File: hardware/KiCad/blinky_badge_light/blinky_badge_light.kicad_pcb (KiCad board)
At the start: 4 copper layers, 108.6 x 87.8 mm, 108 parts, among them Q2 Q_PMOS_GSD, SW1 TS-1187A-B-A-B, U1 ESP32-S3-WROOM-1, U2 TP4056, U3 AP2112K-3.3, U4 MT3608, U5 CP2102N-Axx-xQFN24, U6 SN74LVC1T45DBV

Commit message: adding plus and minus to inside battery holder so it's easier to see which direction to use
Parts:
- added G***: LOGO, labels:minus, B.Cu at (119.3, 82.1)
- added G***: LOGO, labels:plus, B.Cu at (180.2, 82.1)
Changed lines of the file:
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@@
+		(embedded_fonts no)
+	)
+	(footprint "labels:minus"
+		(layer "B.Cu")
+		(at 119.251036 82.058777)
+		(property "Reference" "G***"
+			(at 0 0 180)
+			(layer "F.SilkS")
+			(hide yes)
+			(effects
+				(font
+					(size 1.5 1.5)
+					(thickness 0.3)
+				)
+			)
+		)
+		(property "Value" "LOGO"
+			(at 0.75 0 180)
+			(layer "F.SilkS")
+			(hide yes)
+			(effects
+				(font
+					(size 1.5 1.5)
+					(thickness 0.3)
+				)
+			)
+		)
+		(property "Datasheet" ""
+			(at 0 0 180)
+			(layer "B.Fab")
+			(hide yes)
+			(effects
+				(font
+					(size 1.27 1.27)
+					(thickness 0.15)
+				)
+				(justify mirror)
+			)
+		)
+		(property "Description" ""
+			(at 0 0 180)
+			(layer "B.Fab")
+			(hide yes)
+			(effects
+				(font
+					(size 1.27 1.27)
+					(thickness 0.15)
+				)
+				(justify mirror)
+			)
+		)
+		(attr board_only exclude_from_pos_files exclude_from_bom)
+		(fp_poly
+			(pts
+				(xy -0.286687 -0.690521) (xy 0.090711 -0.696229) (xy 1.390739 -0.719666) (xy 1.515832 -0.942743)
+				(xy 1.593212 -1.119444) (xy 1.569107 -1.263259) (xy 1.495844 -1.387243) (xy 1.350762 -1.608666)
+				(xy 0.053503 -1.608666) (xy -0.449903 -1.606654) (xy -0.811495 -1.598645) (xy -1.058768 -1.581677)
+				(xy -1.219213 -1.552788) (xy -1.320324 -1.509018) (xy -1.383879 -1.453832) (xy -1.510433 -1.211294)
+				(xy -1.479872 -0.965652) (xy -1.366659 -0.815185) (xy -1.284805 -0.760109) (xy -1.163403 -0.722351)
+				(xy -0.97493 -0.699665) (xy -0.691865 -0.689803)
+			)
+			(stroke
+				(width 0)
+				(type solid)
+			)
+			(fill yes)
+			(layer "B.SilkS")
+		)
 		(embedded_fonts no)
 	)
@@
 		)
 	)
+	(footprint "labels:plus"
+		(layer "B.Cu")
+		(at 180.21152 82.063129)
+		(property "Reference" "G***"
+			(at 0 0 180)
+			(layer "F.SilkS")
+			(hide yes)
+			(effects
+				(font
+					(size 1.5 1.5)
+					(thickness 0.3)
+				)
+			)
+		)
+		(property "Value" "LOGO"
+			(at 0.75 0 180)
+			(layer "F.SilkS")
+			(hide yes)
+			(effects
+				(font
+					(size 1.5 1.5)
+					(thickness 0.3)
+				)
+			)
+		)
+		(property "Datasheet" ""
+			(at 0 0 180)
+			(layer "B.Fab")
+			(hide yes)
+			(effects
+				(font
+					(size 1.27 1.27)
+					(thickness 0.15)
+				)
+				(justify mirror)
+			)
+		)
+		(property "Description" ""
+			(at 0 0 180)
+			(layer "B.Fab")
+			(hide yes)
+			(effects
+				(font
+					(size 1.27 1.27)
+					(thickness 0.15)
+				)
+				(justify mirror)
+			)
+		)
+		(attr board_only exclude_from_pos_files exclude_from_bom)
+		(fp_poly
+			(pts
+				(xy 0.322711 1.607171) (xy 0.466663 1.523091) (xy 0.562701 1.353457) (xy 0.621675 1.074135) (xy 0.654437 0.660986)
+				(xy 0.663657 0.420523) (xy 0.692314 -0.507999) (xy 1.560701 -0.507999) (xy 1.968384 -0.51241) (xy 2.241811 -0.529217)
+				(xy 2.415912 -0.563784) (xy 2.525616 -0.621474) (xy 2.56921 -0.662833) (xy 2.695614 -0.904885) (xy 2.666152 -1.149983)
+				(xy 2.554499 -1.29921) (xy 2.443165 -1.366708) (xy 2.266689 -1.409464) (xy 1.991479 -1.432114) (xy 1.583946 -1.439288)
+				(xy 1.538499 -1.439333) (xy 0.677333 -1.439333) (xy 0.676084 -2.264833) (xy 0.663726 -2.695063)
+				(xy 0.630758 -3.043722) (xy 0.581262 -3.271525) (xy 0.56832 -3.301999) (xy 0.395917 -3.480139) (xy 0.155788 -3.546055)
+				(xy -0.085557 -3.490747) (xy -0.194827 -3.405274) (xy -0.261988 -3.298771) (xy -0.305231 -3.135068)
+				(xy -0.329105 -2.880577) (xy -0.338158 -2.501709) (xy -0.338667 -2.342832) (xy -0.338667 -1.439333)
+				(xy -1.259634 -1.439333) (xy -1.720069 -1.432163) (xy -2.037288 -1.403587) (xy -2.237063 -1.343005)
+				(xy -2.345167 -1.239817) (xy -2.387371 -1.083422) (xy -2.391834 -0.973666) (xy -2.374402 -0.784292)
+				(xy -2.304924 -0.653822) (xy -2.157627 -0.571656) (xy -1.90674 -0.527193) (xy -1.526491 -0.509835)
+				(xy -1.259634 -0.507999) (xy -0.338667 -0.507999) (xy -0.338667 0.407152) (xy -0.329193 0.894518)
+				(xy -0.294911 1.23673) (xy -0.227037 1.457207) (xy -0.116785 1.57937) (xy 0.044629 1.626638) (xy 0.119995 1.629834)
+			)
+			(stroke
+				(width 0)
+				(type solid)
+			)
+			(fill yes)
+			(layer "B.SilkS")
+		)
+		(embedded_fonts no)
+	)
 	(footprint "Capacitor_SMD:C_0402_1005Metric"

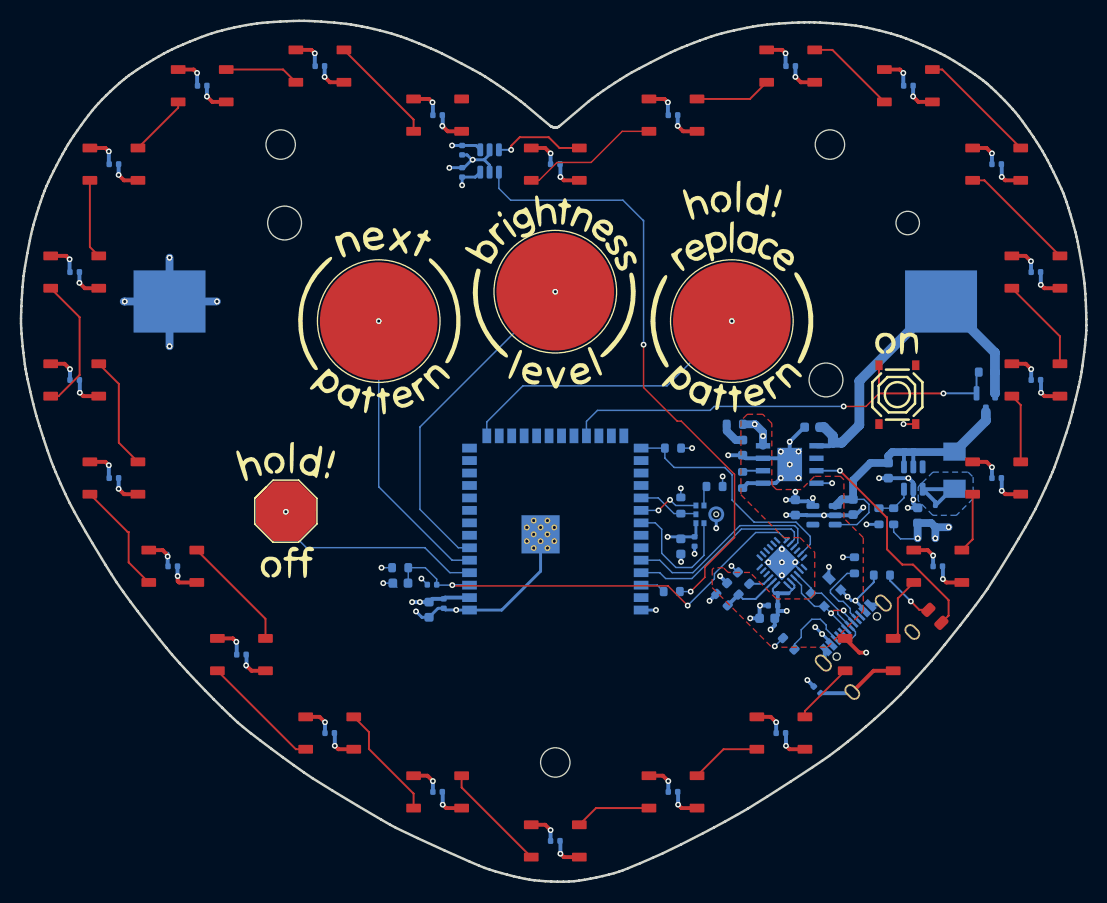
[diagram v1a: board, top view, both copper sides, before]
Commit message: fix symbol used by transistor
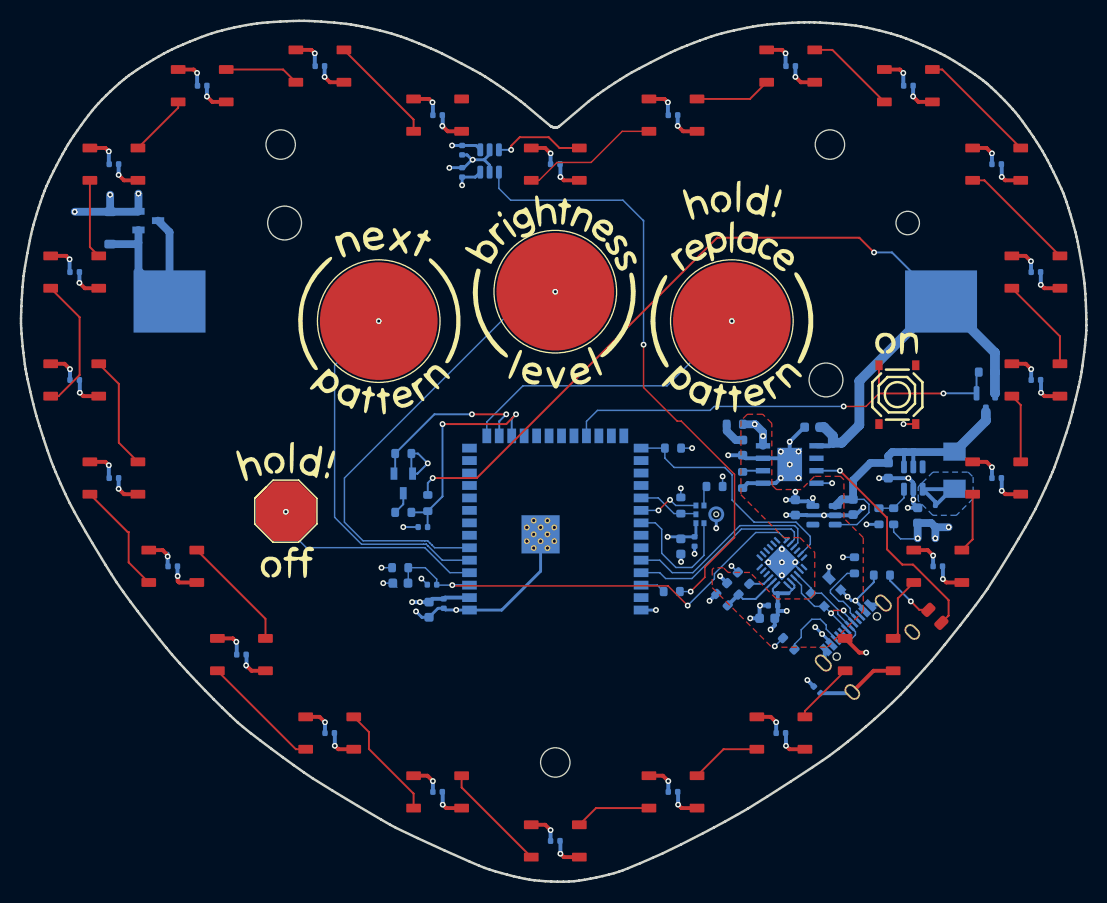
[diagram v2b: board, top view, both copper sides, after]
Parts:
- removed the G*** at (125.0, 98.5)
- added C41: 100nF, Capacitor_SMD:C_0402_1005Metric, B.Cu at (136.5, 104.0)
- added D28: ESD Diode, Diode_SMD:D_SOD-123, B.Cu at (104.6, 73.5)
- added Q1: N-Channel MOSFET, footprints:SOT-23-3_L2.9-W1.3-P1.90-LS2.4-BR, B.Cu at (108.5, 72.8)
- added Q3: N-Channel MOSFET, footprints:SOT-23-3_L2.9-W1.3-P1.90-LS2.4-BR, B.Cu at (134.5, 99.5)
- added R13: 100kΩ, Resistor_SMD:R_0603_1608Metric, B.Cu at (137.0, 101.5)
- added R18: 100kΩ, Resistor_SMD:R_0603_1608Metric, B.Cu at (134.5, 102.5)
- added R19: 100kΩ, Resistor_SMD:R_0603_1608Metric, B.Cu at (134.5, 96.5)
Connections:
- BT1 pad 2: GND -> BAT-
- U1 pad 16: unconnected-(U1-GPIO46-Pad16) -> ESP32 Battery Monitoring Control
- U1 pad 17: unconnected-(U1-GPIO9/TOUCH9/ADC1_CH8/FSPIHD/SUBSPIHD-Pad17) -> ESP32 Battery Monitoring
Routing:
- net BAT+: track 35.3 -> 101.9 mm, vias 0 -> 2
- net ESP32 Battery Monitoring: track 0.00 -> 23.2 mm, vias 0 -> 2
- net BAT-: track 0.00 -> 20.1 mm
- net ESP32 Battery Monitoring Control: track 0.00 -> 17.6 mm, vias 0 -> 2
- net Net-(U1-GPIO6/TOUCH6/ADC1_CH5): track 34.6 -> 47.7 mm
- net Net-(U1-GPIO5/TOUCH5/ADC1_CH4): track 29.2 -> 37.4 mm
- net Net-(Q3-D): track 0.00 -> 2.29 mm
- net GND: track 182.2 -> 181.4 mm, vias 66 -> 67

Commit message: moving some stuff around
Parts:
- added TOUCH_5: TestPoint, TestPoint:TestPoint_Pad_D4.0mm, F.Cu at (114.0, 93.0)
- moved Q3 62.4 mm to (186.5, 65.0)
- moved R19 62.4 mm to (186.5, 62.0)
- moved R18 61.4 mm to (185.0, 67.5), turned to 90 degrees
- moved R13 61.3 mm to (188.0, 67.5)
- moved C41 61.3 mm to (186.5, 68.5), turned to 90 degrees
- moved G*** 6.20 mm to (127.1, 106.3)
- moved TOUCH_4 6.20 mm to (126.5, 106.5)
- moved G*** 1.50 mm to (149.5, 81.5)
- moved TOUCH_2 1.50 mm to (150.0, 81.5)
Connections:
- U1 pad 7: unconnected-(U1-GPIO7/TOUCH7/ADC1_CH6-Pad7) -> Net-(U1-GPIO7/TOUCH7/ADC1_CH6)
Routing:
- net BAT+: track 101.9 -> 52.0 mm, vias 2 -> 0
- net ESP32 Battery Monitoring Control: track 17.6 -> 65.4 mm
- net ESP32 Battery Monitoring: track 23.2 -> 60.0 mm
- net Net-(U1-GPIO7/TOUCH7/ADC1_CH6): track 0.00 -> 32.2 mm, vias 0 -> 3
- net Net-(U1-GPIO6/TOUCH6/ADC1_CH5): track 47.7 -> 38.6 mm
- net Net-(U1-GPIO5/TOUCH5/ADC1_CH4): track 37.4 -> 30.5 mm
- net Net-(U1-GPIO4/TOUCH4/ADC1_CH3): track 22.2 -> 15.3 mm
- net GND: track 181.4 -> 179.1 mm, vias 67 -> 68
- net Net-(Q3-D): track 2.29 -> 1.78 mm

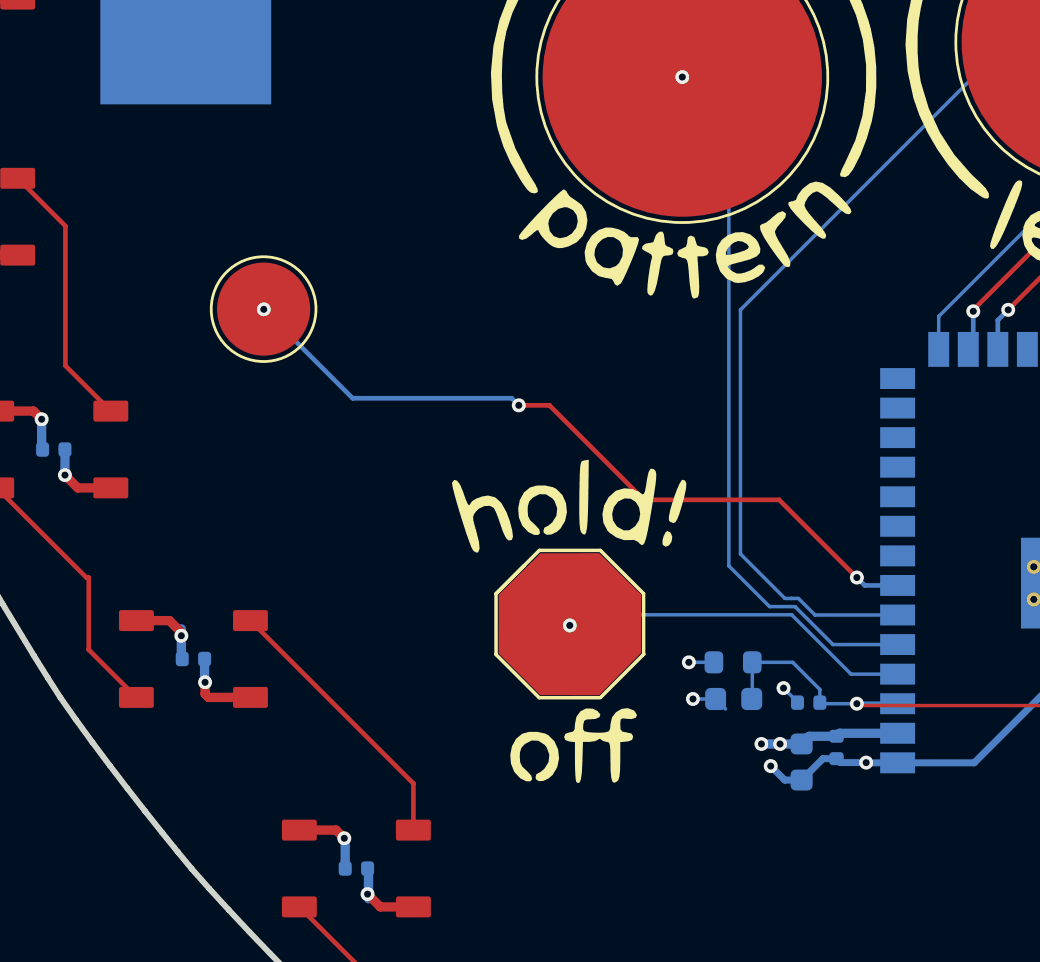
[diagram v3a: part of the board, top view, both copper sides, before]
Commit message: adding two new touch pads
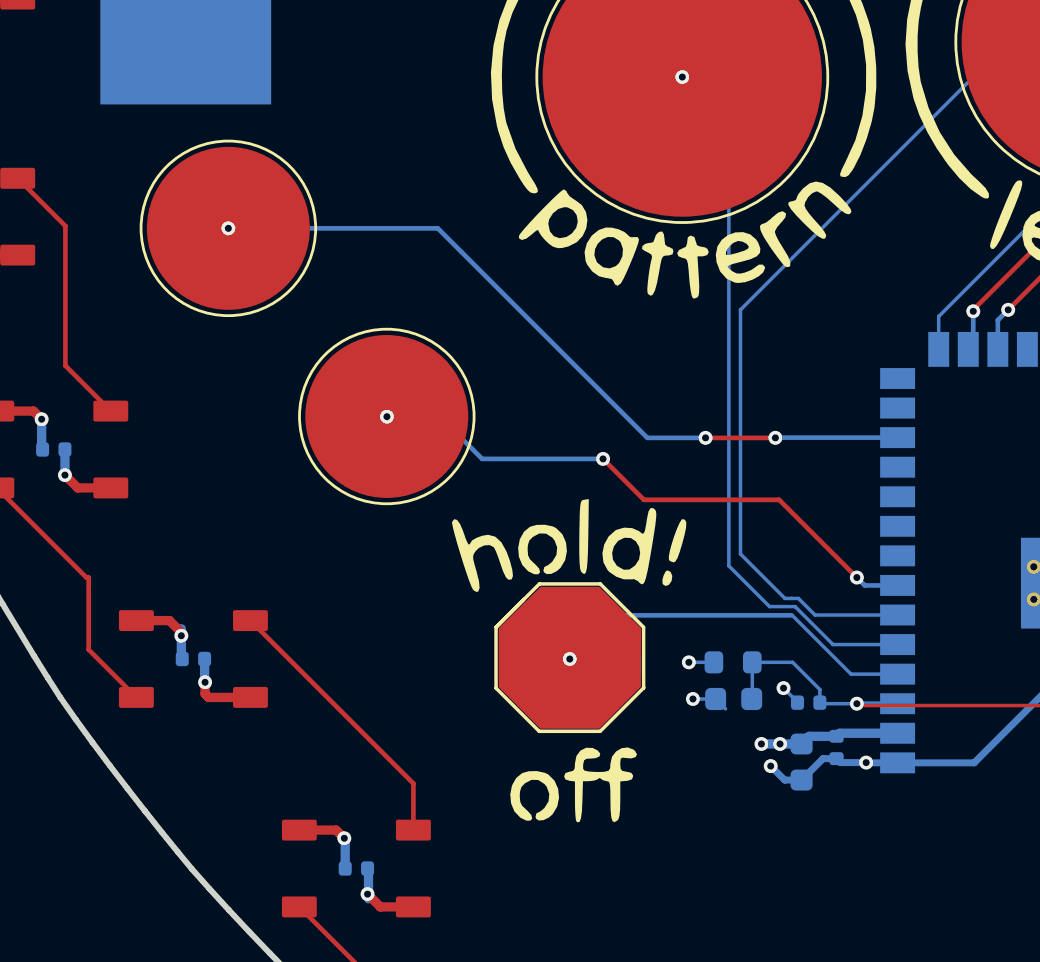
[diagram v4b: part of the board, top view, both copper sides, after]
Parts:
- added TOUCH_6: TestPoint, footprints:TestPoint_Pad_D7.0mm, F.Cu at (112.5, 89.5)
- TOUCH_5: footprint TestPoint:TestPoint_Pad_D4.0mm -> footprints:TestPoint_Pad_D7.0mm
- moved TOUCH_5 7.02 mm to (119.3, 97.6)
- moved G*** 1.69 mm to (127.1, 108.0)
- moved TOUCH_4 1.44 mm to (126.5, 107.9)
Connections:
- U1 pad 12: unconnected-(U1-GPIO8/TOUCH8/ADC1_CH7/SUBSPICS1-Pad12) -> Net-(U1-GPIO8/TOUCH8/ADC1_CH7/SUBSPICS1)
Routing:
- net Net-(U1-GPIO8/TOUCH8/ADC1_CH7/SUBSPICS1): track 0.00 -> 32.5 mm, vias 0 -> 3
- net Net-(U1-GPIO7/TOUCH7/ADC1_CH6): track 32.2 -> 25.0 mm
- net Net-(U1-GPIO4/TOUCH4/ADC1_CH3): track 15.3 -> 15.9 mm

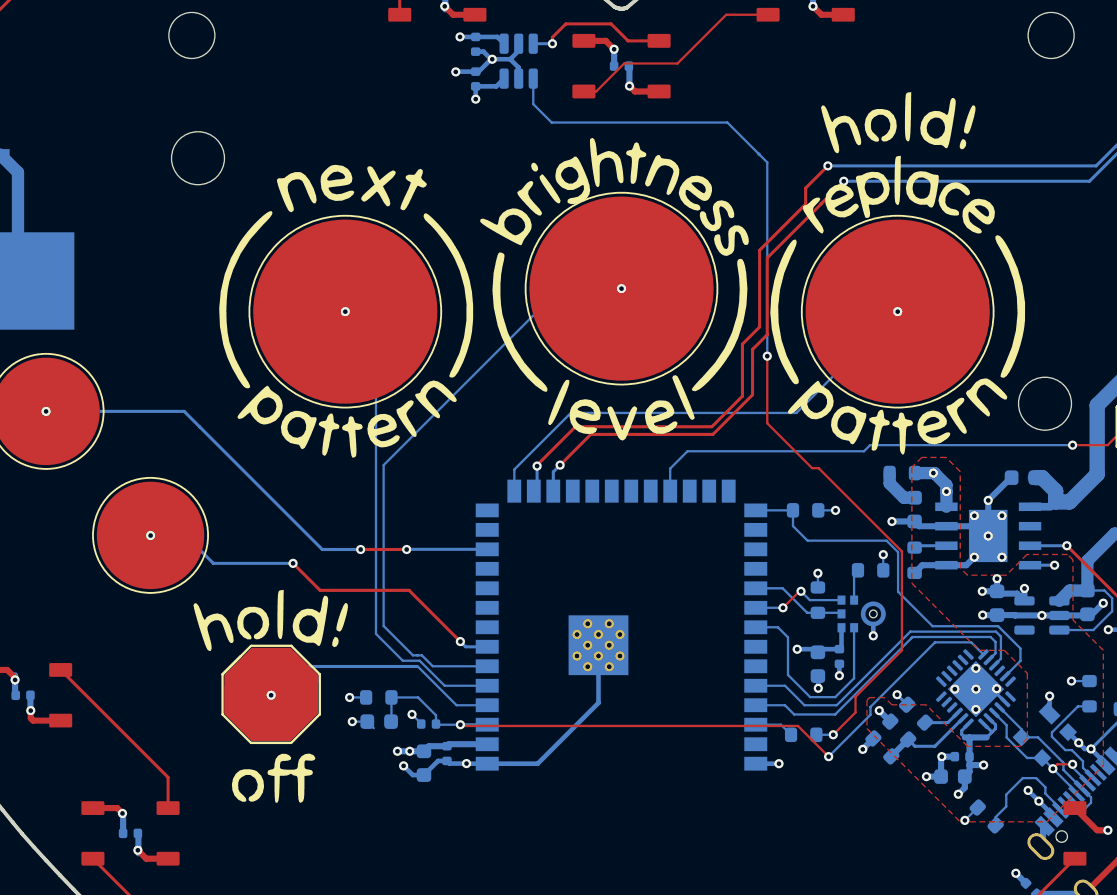
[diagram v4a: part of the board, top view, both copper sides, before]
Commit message: new labels, new pads
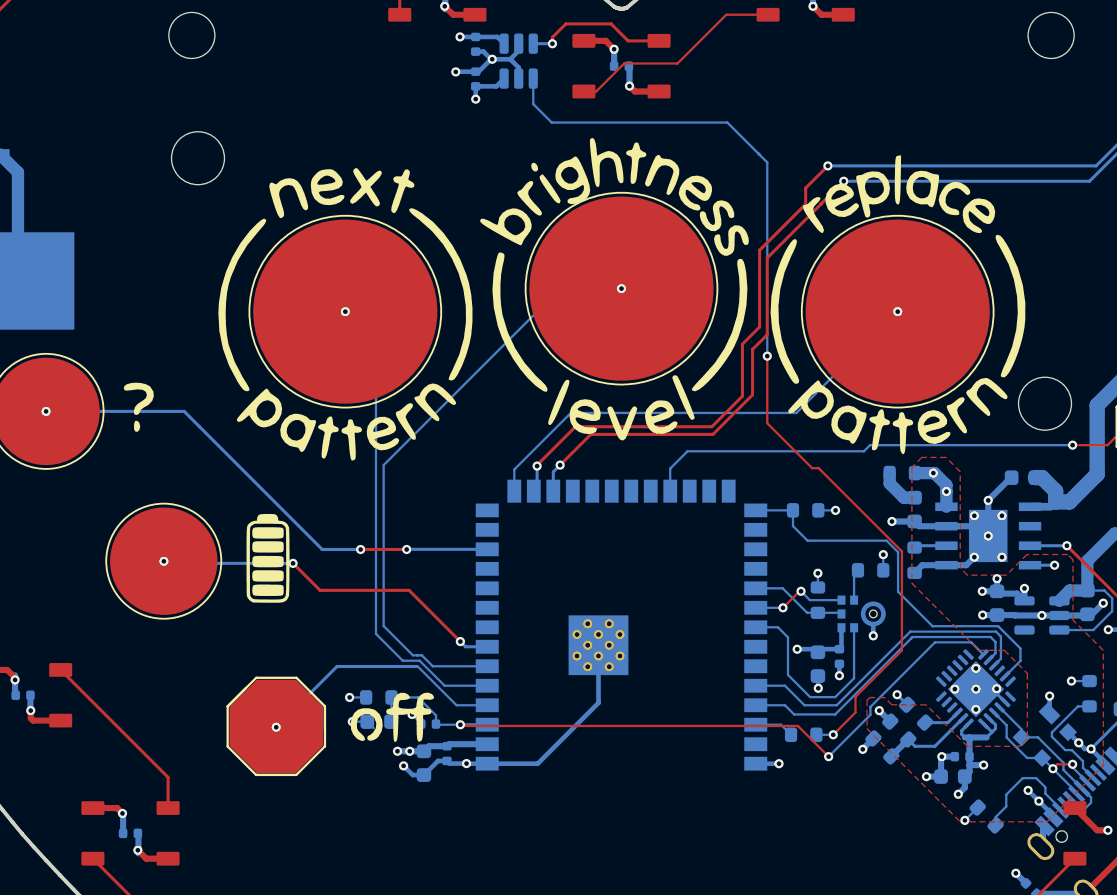
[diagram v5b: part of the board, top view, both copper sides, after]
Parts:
- removed the G*** at (127.1, 108.0)
- removed the G*** at (168.1, 82.6)
- added G***: LOGO, labels:off, F.Cu at (134.9, 104.0)
- added G***: LOGO, labels:replace_pattern_2, F.Cu at (167.4, 80.6)
- added G***: LOGO, labels:questionmark, F.Cu at (118.3, 88.9)
- added G***: LOGO, labels:battery, F.Cu at (126.5, 99.4)
- moved TOUCH_4 2.11 mm to (126.8, 110.0)
- moved TOUCH_5 1.89 mm to (120.2, 99.3)
- moved G*** 0.19 mm to (132.0, 83.2)
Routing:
- net Net-(U1-GPIO7/TOUCH7/ADC1_CH6): track 25.0 -> 23.5 mm
- net Net-(U1-GPIO4/TOUCH4/ADC1_CH3): track 15.9 -> 16.4 mm

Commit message: hanger ring
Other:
- board size 108.6 x 87.8 mm -> 108.6 x 87.7 mm
